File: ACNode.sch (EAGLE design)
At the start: 55 parts, among them IC1 74AHC1G04DCK, IC2 MC78M05CDTG, IC3 LM1117IMP-3.3, U2 MAGJACK-POE, Y1 25mhz, Y2 20mhz

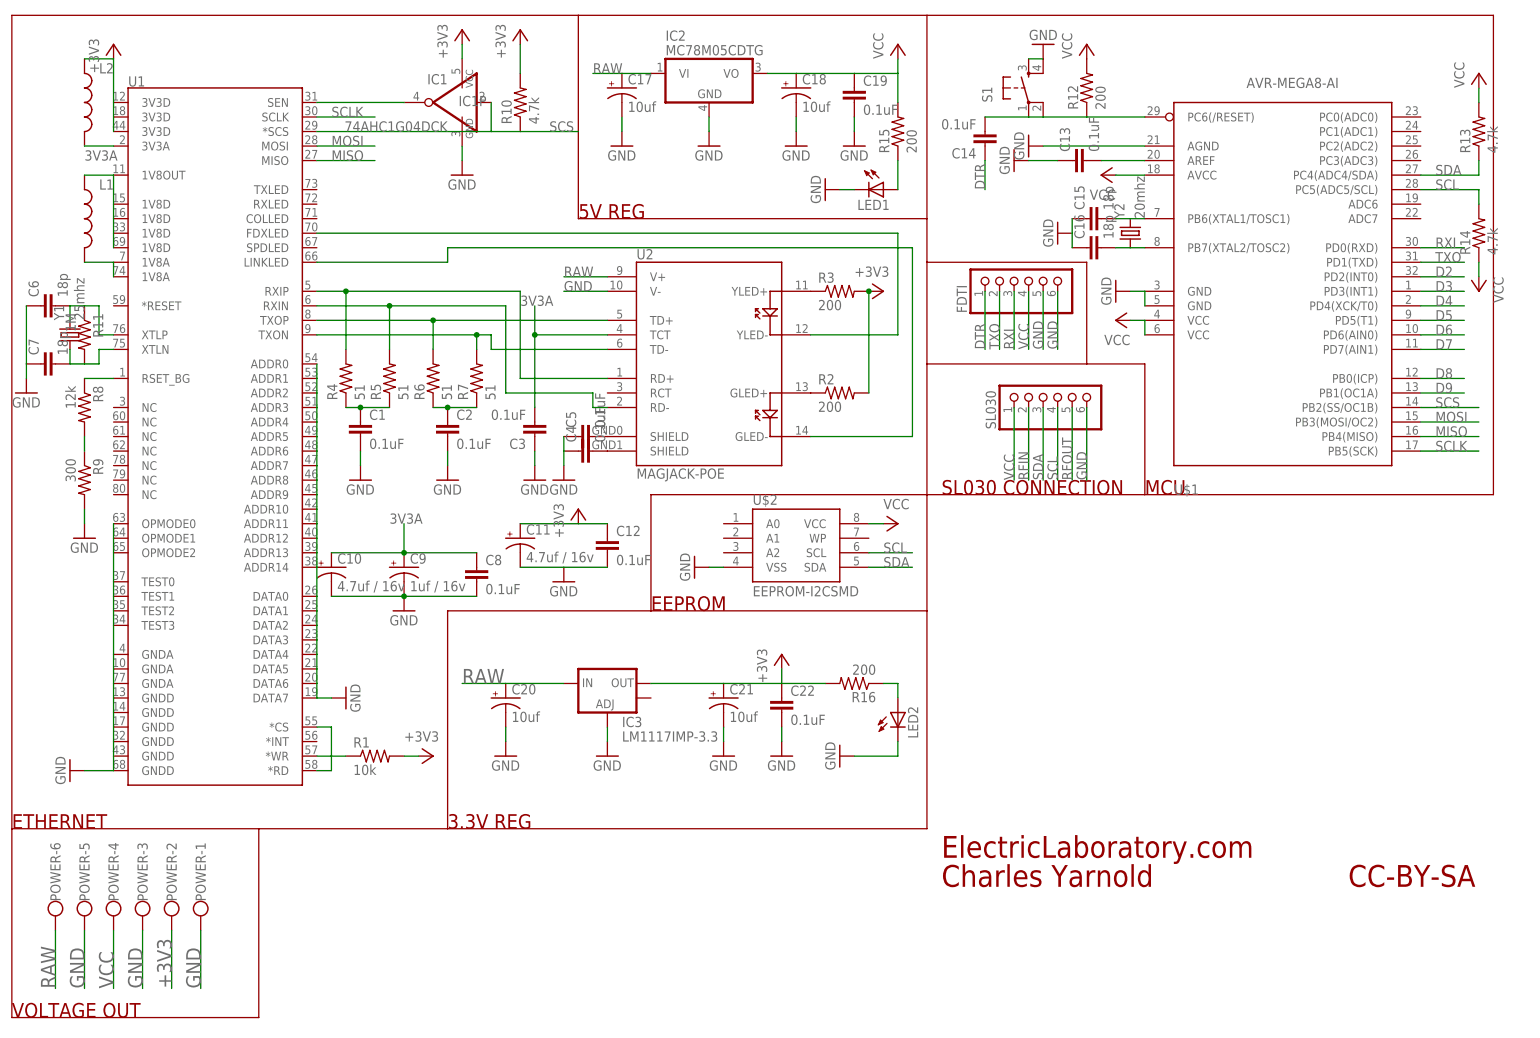
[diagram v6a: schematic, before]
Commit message: Add button, led and relay
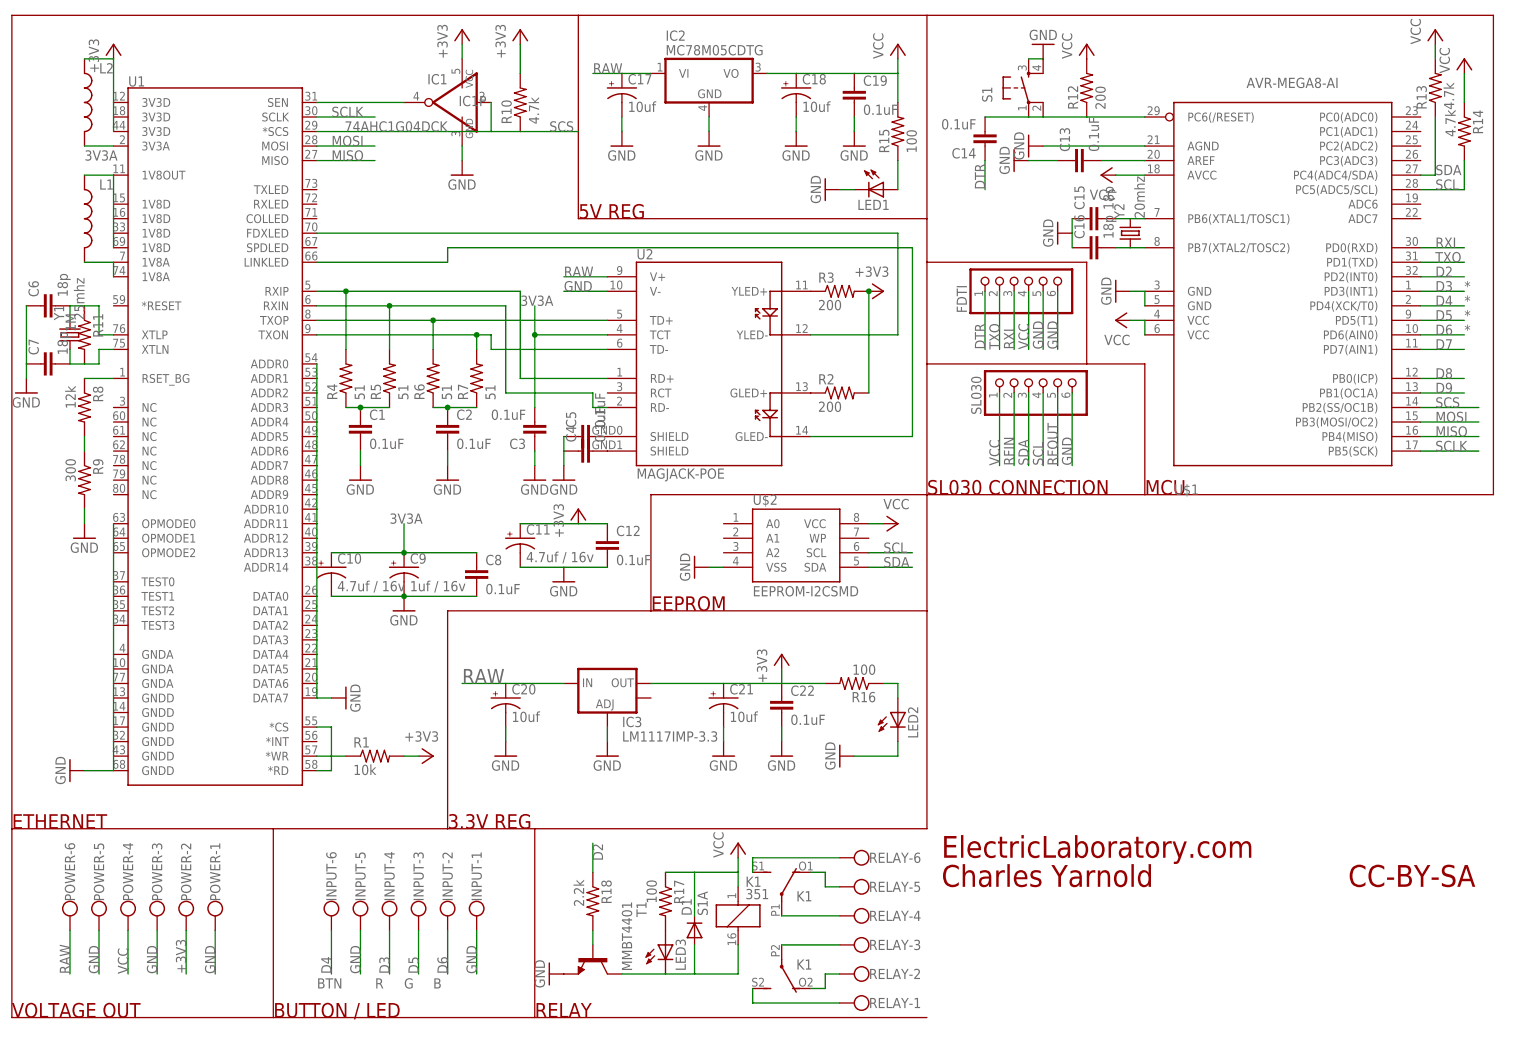
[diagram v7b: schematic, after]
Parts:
- added D1: S1A, diode:DIODE-DO-214AC
- added INPUT, RELAY: (no value), con-wago-500:W237-6
- added K1: 351, relay:351
- added LED3: (no value), SparkFun-LED:LED0603
- added R17: 100, SparkFun-Passives:RESISTOR0805-RES
- added R18: 2.2k, SparkFun-Passives:RESISTOR0805-RES
- added T1: MMBT4401, transistor:MMBT4401LT1-NPN-SOT23-BEC
- R15, R16: value 200 -> 100
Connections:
- new net N$25: K13.S, RELAY-1.KL
- new net N$27: K13.O, RELAY-2.KL
- new net N$29: K13.P, RELAY-3.KL
- new net N$30: K12.P, RELAY-4.KL
- new net N$31: K12.O, RELAY-5.KL
- new net N$32: K12.S, RELAY-6.KL
- new net N$33: LED3.A, R17.2
- new net N$34: D1.A, K11.2, LED3.C, T1.C
- new net N$35: R18.2, T1.B
- net D2: now also R18.1
- net D3: now also INPUT-4.KL
- net D4: now also INPUT-6.KL
- net D5: now also INPUT-3.KL
- net D6: now also INPUT-2.KL
- net GND: now also INPUT-1.KL, INPUT-5.KL, T1.E
- net VCC: now also D1.C, K11.1, R17.1
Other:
- note added: "*"
- note added: "B"
- note added: "BTN"
- note added: "BUTTON / LED"
- note added: "G"
- note added: "R"
- note added: "RELAY"
- moved on the sheet: POWER-1, POWER-2, POWER-3, POWER-4, POWER-5, POWER-6, R13, R14, SL030

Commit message: Add controls, tidy up, add w5100 reset
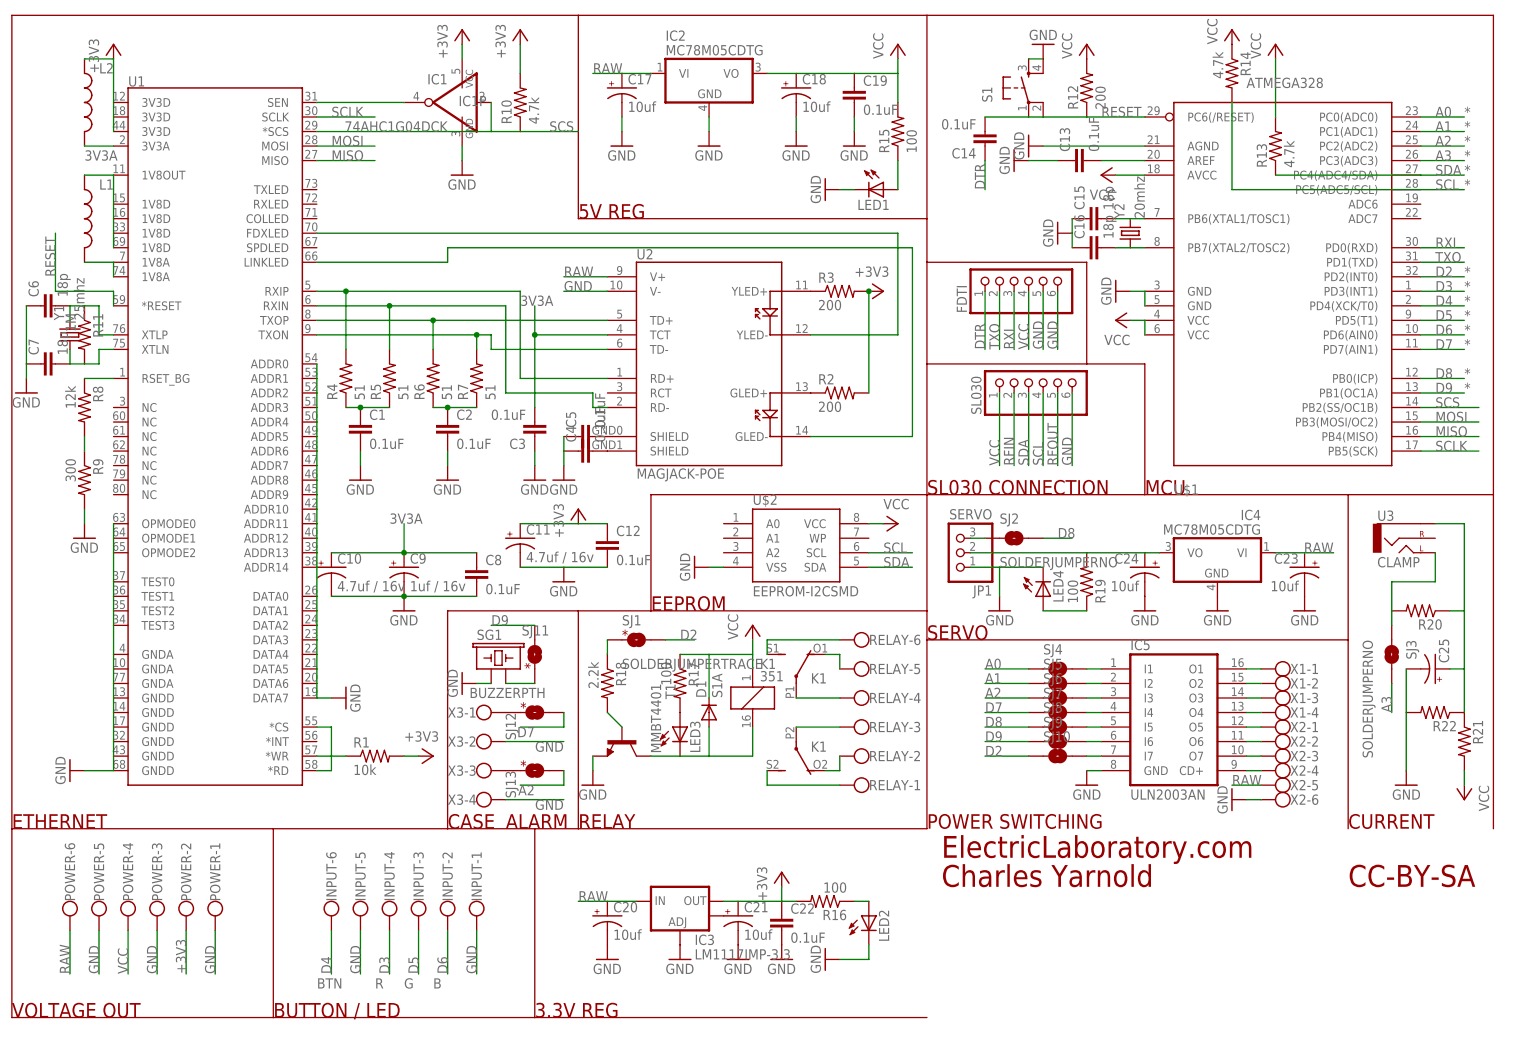
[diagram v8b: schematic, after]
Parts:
- added C23, C24: 10uf, SparkFun-Passives:CAP_POL1206
- added C25: (no value), SparkFun-Passives:CAP_POL1206
- added IC4: MC78M05CDTG, linear:MC78M05CDTG
- added IC5: ULN2003AN, uln-udn:ULN2003AN
- added JP1: SERVO, pinhead:PINHD-1X3
- added LED4: (no value), SparkFun-LED:LED0603
- added R19: 100, SparkFun-Passives:RESISTOR0603-RES
- added R20, R21, R22: (no value), SparkFun-Passives:RESISTOR0603-RES
- added SG1: BUZZERPTH, SparkFun-Electromechanical:BUZZERPTH
- added SJ1, SJ11, SJ12, SJ13: SOLDERJUMPERTRACE, SparkFun-Passives:SOLDERJUMPERTRACE
- added SJ10, SJ2, SJ3, SJ4, SJ5, SJ6, SJ7, SJ8, SJ9: SOLDERJUMPERNO, SparkFun-Passives:SOLDERJUMPERNO
- added U3: CLAMP, SparkFun-Connectors:AUDIO-JACKPTH
- added X1, X3: (no value), con-wago-500:W237-4
- added X2: (no value), con-wago-500:W237-6
- U$1: value AVR-MEGA8-AI -> ATMEGA328
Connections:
- removed net N$23: C14.2, R12.1, S1.1, S1.2, U$1.PC6(/RESET)
- new net A0: SJ4.1, U$1.PC0(ADC0)
- new net A1: SJ5.1, U$1.PC1(ADC1)
- new net A2: SJ13.2, SJ6.1, U$1.PC2(ADC2)
- new net A3: SJ3.2, U$1.PC3(ADC3)
- new net N$36: LED4.A, R19.1
- new net N$37: R18.1, SJ1.1
- new net N$38: C24.+, IC4.VO, JP1.2, R19.2
- new net N$39: JP1.3, SJ2.1
- new net N$40: C25.+, R20.1, R21.1, R22.1, U3.SLEEVE
- new net N$41: R20.2, SJ3.1, U3.LEFT
- new net N$42: IC5.O1, X1-1.KL
- new net N$43: IC5.O2, X1-2.KL
- new net N$44: IC5.O3, X1-3.KL
- new net N$45: IC5.O4, X1-4.KL
- new net N$46: IC5.O5, X2-1.KL
- new net N$47: IC5.O6, X2-2.KL
- new net N$48: IC5.O7, X2-3.KL
- new net N$49: IC5.CD+, X2-4.KL
- new net N$50: IC5.I7, SJ10.2
- new net N$51: IC5.I6, SJ9.2
- new net N$52: IC5.I5, SJ8.2
- new net N$53: IC5.I4, SJ7.2
- new net N$54: IC5.I3, SJ6.2
- new net N$55: IC5.I2, SJ5.2
- new net N$56: IC5.I1, SJ4.2
- new net N$57: SG1.2, SJ11.2
- new net N$58: SJ12.1, X3-1.KL
- new net N$59: SJ13.1, X3-3.KL
- new net RESET: C14.2, R12.1, S1.1, S1.2, U$1.PC6(/RESET), U1.*RESET
- net D2: now also SJ1.2, SJ10.1; no longer R18.1
- net D7: now also SJ12.2, SJ7.1
- net D8: now also SJ2.2, SJ8.1
- net D9: now also SJ11.1, SJ9.1
- net GND: now also C23.-, C24.-, C25.-, IC4.GND, IC5.GND, JP1.1, LED4.C, R22.2, SG1.1, X2-6.KL, X3-2.KL, X3-4.KL
- net RAW: now also C23.+, IC4.VI, X2-5.KL
- net VCC: now also R21.2
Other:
- note added: "ALARM"
- note added: "CASE"
- note added: "CURRENT"
- note added: "POWER SWITCHING"
- note added: "SERVO"
- moved on the sheet: C20, C21, C22, D1, IC3, K1, LED2, LED3, R13, R14, R16, R17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
